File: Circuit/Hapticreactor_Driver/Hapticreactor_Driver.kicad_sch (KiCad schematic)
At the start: 4 parts

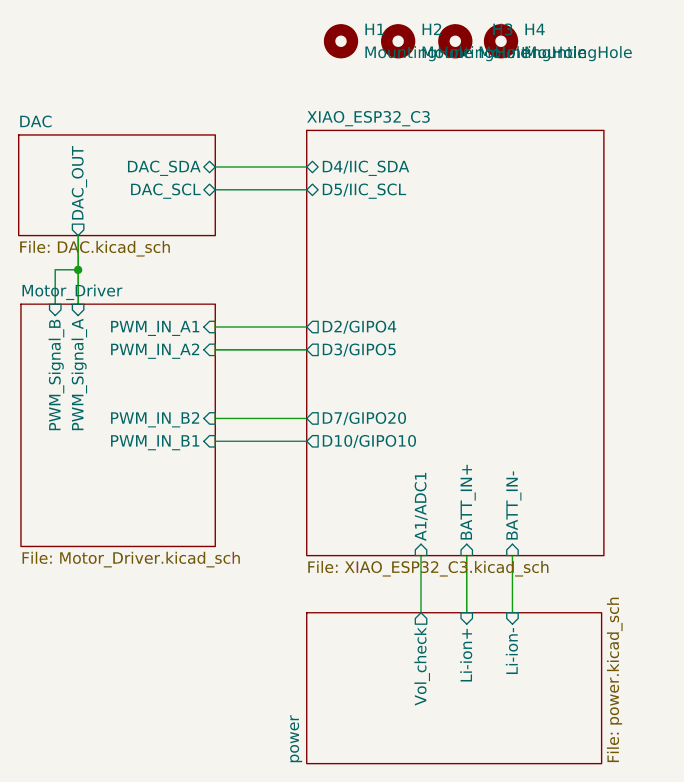
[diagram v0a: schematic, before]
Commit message: 秋野の回路に昇圧DCDCつけて東芝MDつけた
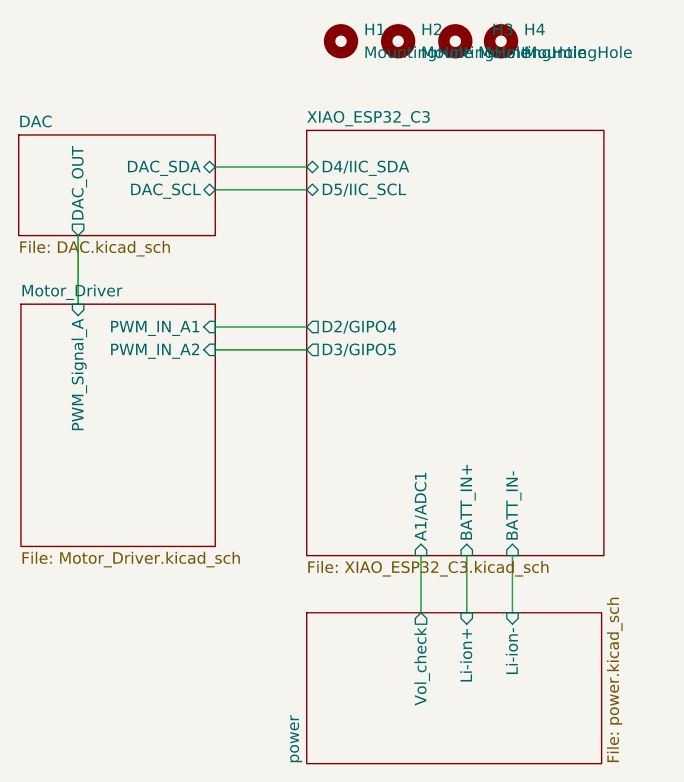
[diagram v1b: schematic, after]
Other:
- sheet Motor_Driver ports: added none; removed PWM_IN_B1, PWM_IN_B2, PWM_Signal_B
- sheet XIAO_ESP32_C3 ports: added none; removed D10/GIPO10, D7/GIPO20
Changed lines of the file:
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@@
 	(generator_version "9.0")
 	(paper "A4")
-	(junction
-		(at 81.28 72.39)
-		(diameter 0)
-		(color 0 0 0 0)
-	)
-	(wire
-		(pts
-			(xy 78.74 72.39) (xy 81.28 72.39)
-		)
-		(stroke
-			(width 0)
-			(type default)
-		)
-	)
 	(wire
 		(pts
@@
 	(wire
 		(pts
-			(xy 96.52 91.44) (xy 106.68 91.44)
-		)
-		(stroke
-			(width 0)
-			(type default)
-		)
-	)
-	(wire
-		(pts
 			(xy 96.52 78.74) (xy 106.68 78.74)
 		)
@@
 	(wire
 		(pts
-			(xy 96.52 88.9) (xy 106.68 88.9)
-		)
-		(stroke
-			(width 0)
-			(type default)
-		)
-	)
-	(wire
-		(pts
-			(xy 78.74 72.39) (xy 78.74 76.2)
-		)
-		(stroke
-			(width 0)
-			(type default)
-		)
-	)
-	(wire
-		(pts
 			(xy 119.38 104.14) (xy 119.38 110.49)
 		)
@@
 	(wire
 		(pts
-			(xy 81.28 72.39) (xy 81.28 76.2)
+			(xy 81.28 68.58) (xy 81.28 76.2)
 		)
 		(stroke
@@
 		(pts
 			(xy 96.52 81.28) (xy 106.68 81.28)
-		)
-		(stroke
-			(width 0)
-			(type default)
-		)
-	)
-	(wire
-		(pts
-			(xy 81.28 68.58) (xy 81.28 72.39)
 		)
 		(stroke
@@
 			)
 		)
-		(pin "D10{slash}GIPO10" output
-			(at 106.68 91.44 180)
-			(effects
-				(font
-					(size 1.27 1.27)
-				)
-				(justify left)
-			)
-		)
 		(pin "D3{slash}GIPO5" output
 			(at 106.68 81.28 180)
@@
 		(pin "D4{slash}IIC_SDA" bidirectional
 			(at 106.68 60.96 180)
-			(effects
-				(font
-					(size 1.27 1.27)
-				)
-				(justify left)
-			)
-		)
-		(pin "D7{slash}GIPO20" output
-			(at 106.68 88.9 180)
 			(effects
 				(font
@@
 			(effects
 				(font
-					(size 1.27 1.27)
-				)
-				(justify right)
-			)
-		)
-		(pin "PWM_IN_B1" input
-			(at 96.52 91.44 0)
-			(effects
-				(font
-					(size 1.27 1.27)
-				)
-				(justify right)
-			)
-		)
-		(pin "PWM_IN_B2" input
-			(at 96.52 88.9 0)
-			(effects
-				(font
-					(size 1.27 1.27)
-				)
-				(justify right)
-			)
-		)
-		(pin "PWM_Signal_B" input
-			(at 78.74 76.2 90)
-			(effects
-				(font
